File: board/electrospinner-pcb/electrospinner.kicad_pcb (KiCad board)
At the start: 2 copper layers, 28 parts, among them U1 FT230XS, U2 A4988SETTR-T, U3 MSP430G2553IPW20

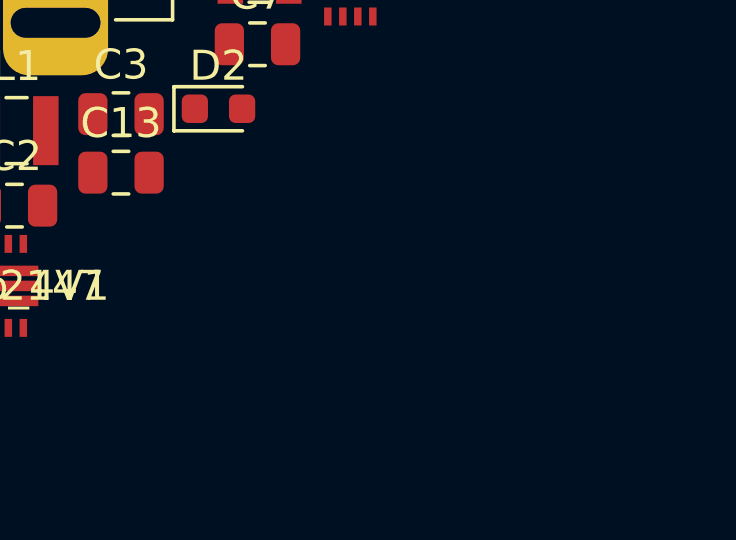
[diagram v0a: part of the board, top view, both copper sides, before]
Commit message: Adds last of the footprints to pcb layout
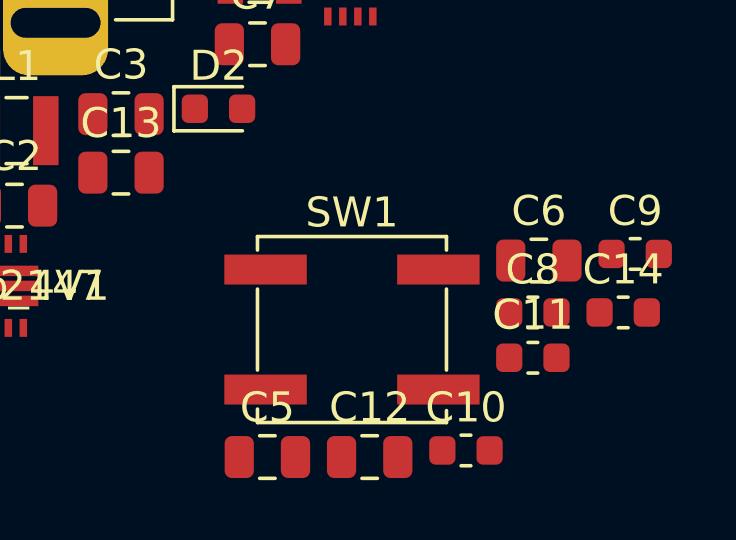
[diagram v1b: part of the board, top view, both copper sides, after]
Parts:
- added C10: 0.1uF, Capacitor_SMD:C_0603_1608Metric, F.Cu at (170.9, 124.1)
- added C11: 0.22uF, Capacitor_SMD:C_0603_1608Metric, F.Cu at (173.1, 121.1)
- added C12: 1uF, Capacitor_SMD:C_0805_2012Metric, F.Cu at (167.7, 124.4)
- added C14: 0.1uF, Capacitor_SMD:C_0603_1608Metric, F.Cu at (176.1, 119.5)
- added C5: 3.3uF, Capacitor_SMD:C_0805_2012Metric, F.Cu at (164.3, 124.4)
- added C6: 3.3uF, Capacitor_SMD:C_0805_2012Metric, F.Cu at (173.3, 117.8)
- added C8: 0.1uF, Capacitor_SMD:C_0603_1608Metric, F.Cu at (173.1, 119.5)
- added C9: 0.1uF, Capacitor_SMD:C_0603_1608Metric, F.Cu at (176.5, 117.6)
- added SW1: ResetBTN, Button_Switch_SMD:SW_SPST_EVPBF, F.Cu at (167.1, 120.1)

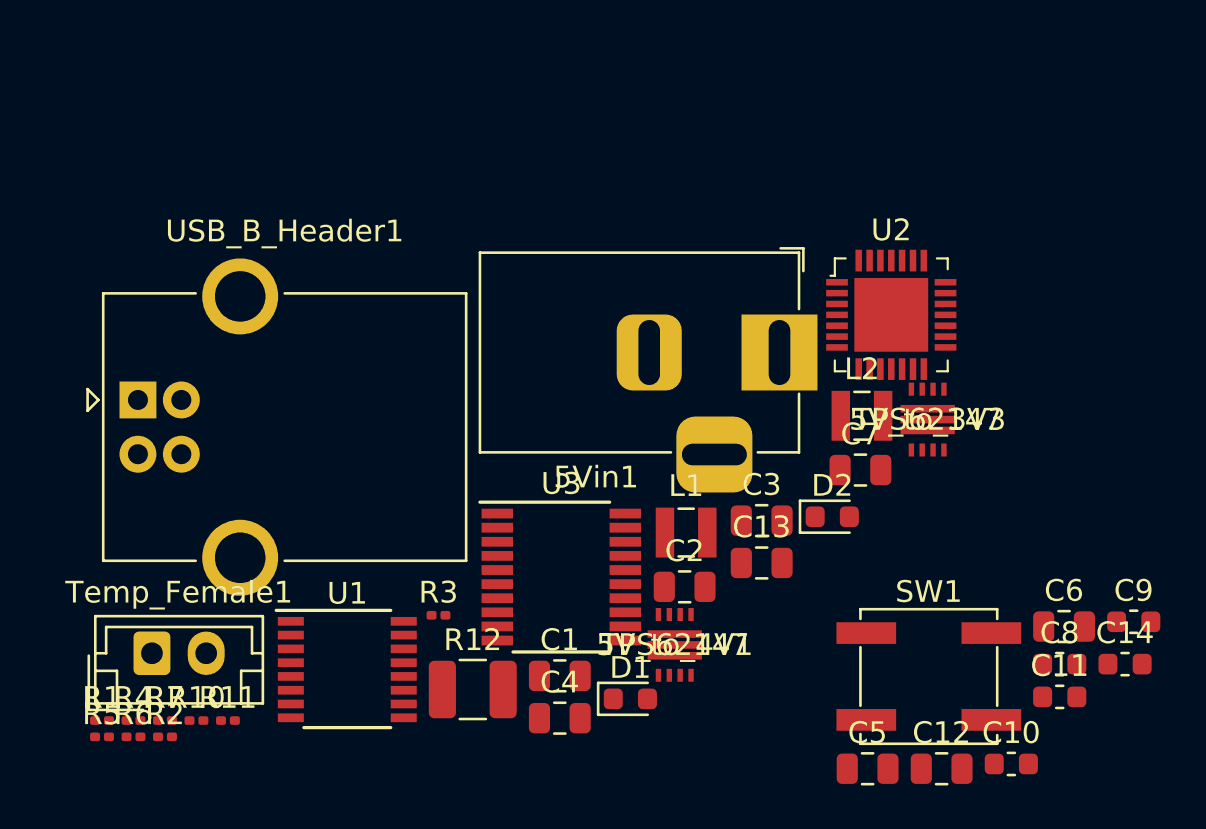
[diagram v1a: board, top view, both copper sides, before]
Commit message: Removes sense resistors from stepper driver
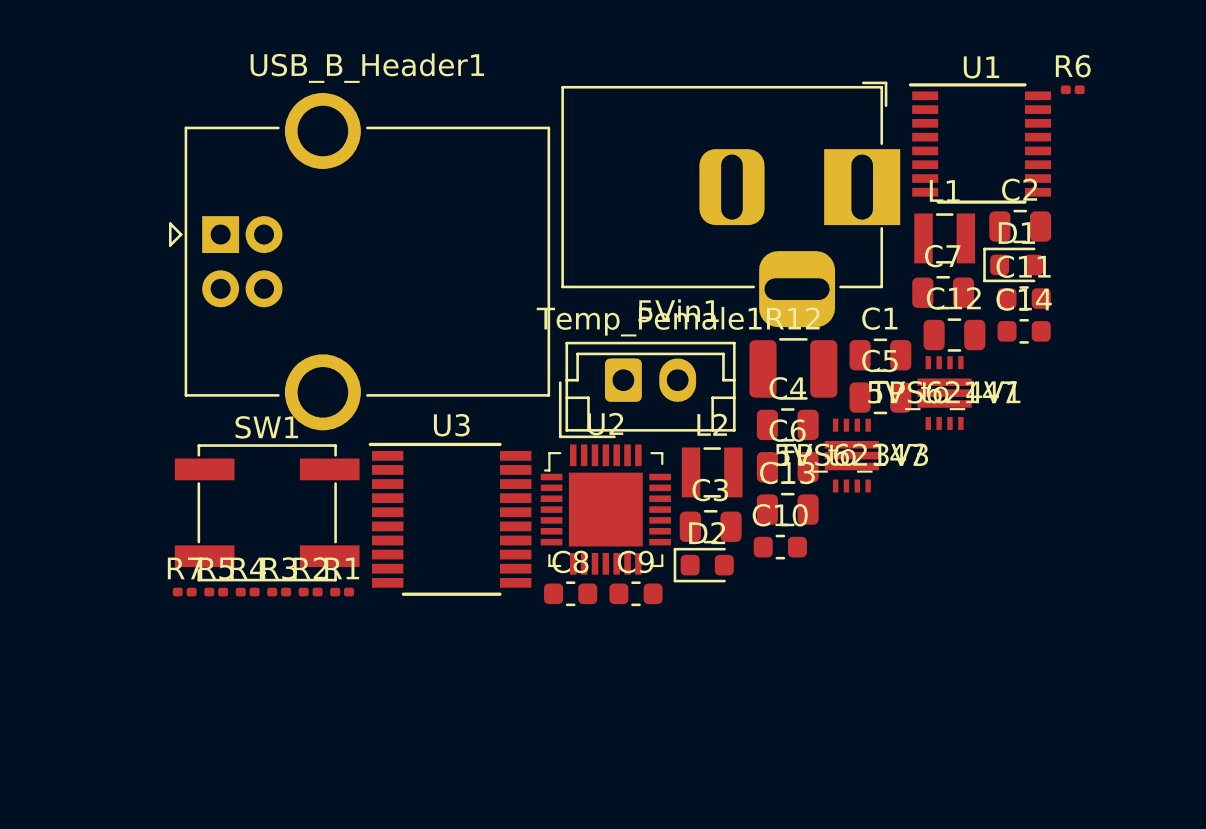
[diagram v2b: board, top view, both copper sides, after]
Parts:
- removed R10, R11: ?k, Resistor_SMD:R_0201_0603Metric
- moved R6 52.5 mm to (173.7, 93.1)
- moved U1 37.9 mm to (169.5, 95.6)
- moved SW1 31.4 mm to (136.6, 112.6)
- moved D1 26.8 mm to (171.1, 101.2)
- moved Temp_Female1 25.1 mm to (153.0, 106.5)
- moved C9 23.0 mm to (153.6, 116.3)
- moved C8 22.8 mm to (150.6, 116.3)
- moved C2 22.7 mm to (171.3, 99.4)
- moved R12 20.9 mm to (160.8, 105.9)
- moved C1 20.9 mm to (164.9, 105.3)
- moved C12 20.0 mm to (168.3, 104.4)
- moved C11 18.4 mm to (171.5, 102.7)
- moved L1 18.0 mm to (167.8, 99.9)
- moved C4 17.1 mm to (160.6, 108.5)
- moved C5 17.1 mm to (164.9, 107.3)
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
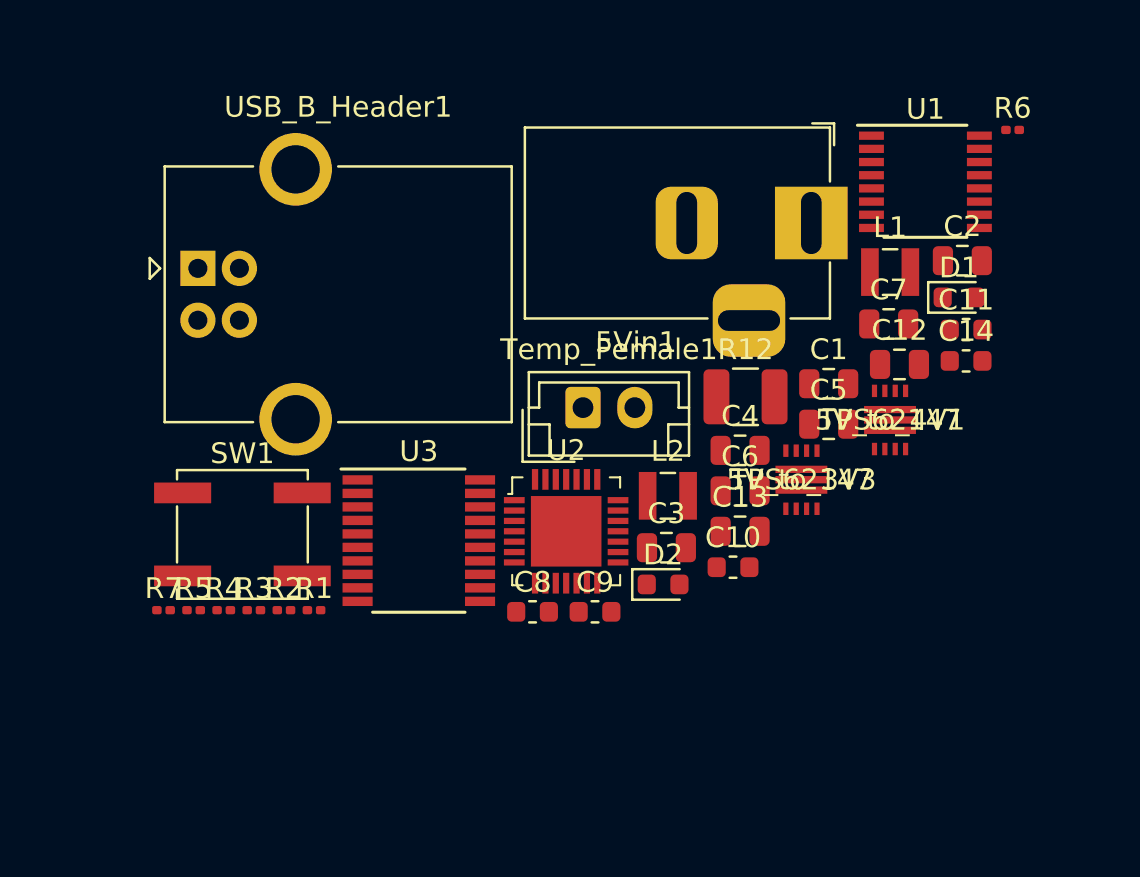
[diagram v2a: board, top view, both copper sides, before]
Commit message: Updates footprints, adds bom
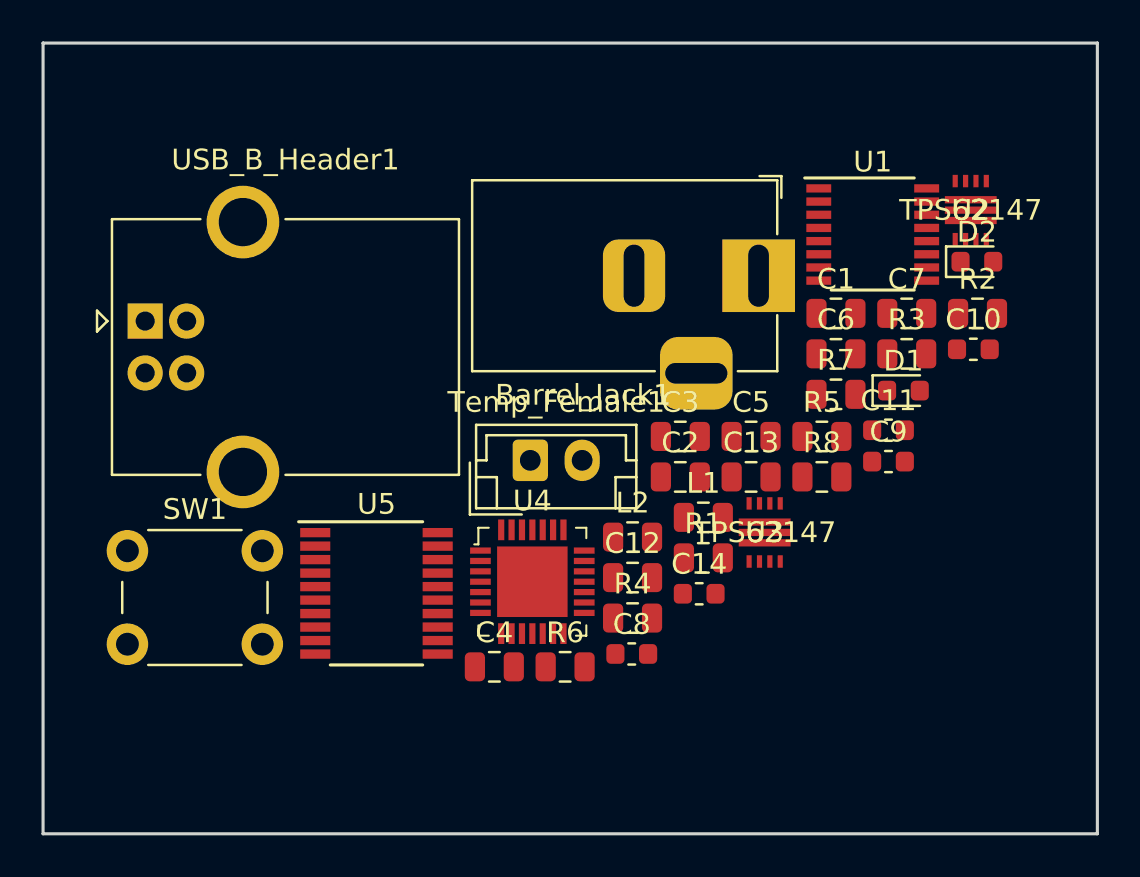
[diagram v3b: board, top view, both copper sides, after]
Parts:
- removed 5V_to_3V3, 5V_to_4V1: TPS62147, footprints:TPS62147RGXR
- removed 5Vin1: BarrelJack, Connector_BarrelJack:BarrelJack_Horizontal
- removed R12: 158, Resistor_SMD:R_1210_3225Metric
- added Barrel_Jack1: BarrelJack, Connector_BarrelJack:BarrelJack_Horizontal, F.Cu at (161.5, 100.1)
- added R8: 158, Resistor_SMD:R_0805_2012Metric, F.Cu at (164.5, 109.8)
- added U4: A4988SETTR-T, digikey-footprints:VFQFN-28-1EP_5x5mm, F.Cu at (150.6, 114.9)
- added U5: MSP430G2553IPW20, Package_SO:TSSOP-20_4.4x6.5mm_P0.65mm, F.Cu at (143.1, 115.4)
- C3, C4: value 2uF -> 3.3uF
- C5, C6: value 3.3uF -> 2uF
- L1, L2: footprint Inductor_SMD:L_Wuerth_MAPI-2510 -> Inductor_SMD:L_0805_2012Metric
- R1: value 560k -> 470k; footprint Resistor_SMD:R_0201_0603Metric -> Resistor_SMD:R_0805_2012Metric
- R2: value 150k -> 100k; footprint Resistor_SMD:R_0201_0603Metric -> Resistor_SMD:R_0805_2012Metric
- R3: value 471k -> 560k; footprint Resistor_SMD:R_0201_0603Metric -> Resistor_SMD:R_0805_2012Metric
- R4: value 100k -> 150k; footprint Resistor_SMD:R_0201_0603Metric -> Resistor_SMD:R_0805_2012Metric
- R5, R6, R7: footprint Resistor_SMD:R_0201_0603Metric -> Resistor_SMD:R_0805_2012Metric
- SW1: footprint Button_Switch_SMD:SW_SPST_EVPBF -> Button_Switch_THT:SW_PUSH_6mm_H5mm
- U2: value A4988SETTR-T -> TPS62147; footprint digikey-footprints:VFQFN-28-1EP_5x5mm -> footprints:TPS62147RGXR
- U3: value MSP430G2553IPW20 -> TPS62147; footprint Package_SO:TSSOP-20_4.4x6.5mm_P0.65mm -> footprints:TPS62147RGXR
- USB_B_Header1: value USB_B -> USB_B_Header?
- moved R2 36.4 mm to (172.0, 101.9)
- moved R7 34.0 mm to (165.2, 105.8)
- moved R3 33.8 mm to (168.6, 103.9)
- moved R6 33.7 mm to (152.2, 119.0)
- moved R5 31.4 mm to (164.5, 107.9)
- moved U2 24.9 mm to (171.7, 96.9)
- moved D2 21.7 mm to (172.0, 99.4)
- moved R4 19.7 mm to (155.4, 116.6)
- moved R1 18.9 mm to (158.8, 113.7)
- moved C2 17.1 mm to (157.7, 109.8)
- moved C14 17.1 mm to (158.6, 115.4)
- moved U3 16.7 mm to (161.8, 112.5)
- moved C12 16.5 mm to (155.4, 114.7)
- moved C9 15.9 mm to (167.7, 109.1)
- moved C4 15.8 mm to (148.7, 119.0)
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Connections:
- C3 pad 1: +3V3 -> Net-(C3-Pad1)
- C4 pad 1: +4V -> Net-(C4-Pad1)
- C5 pad 1: Net-(5V_to_4V1-Pad9) -> +4V
- C6 pad 1: Net-(5V_to_3V3-Pad9) -> +3V3
- L1 pad 1: Net-(5V_to_3V3-Pad2) -> Net-(L1-Pad1)
- L1 pad 2: +3V3 -> +4V
- L2 pad 1: Net-(5V_to_4V1-Pad2) -> Net-(L2-Pad1)
- L2 pad 2: +4V -> +3V3
- R1 pad 1: +3V3 -> +4V
- R1 pad 2: Net-(5V_to_3V3-Pad5) -> Net-(R1-Pad2)
- R2 pad 1: Net-(5V_to_3V3-Pad5) -> Net-(R1-Pad2)
- R3 pad 1: +4V -> +3V3
- R3 pad 2: Net-(5V_to_4V1-Pad5) -> Net-(R3-Pad2)
- R4 pad 1: Net-(5V_to_4V1-Pad5) -> Net-(R3-Pad2)
- U2 pad 1: /2B -> +5V
- U2 pad 10: /MotorMS2 -> GNDD
- U2 pad 11: /MotorMS3 -> +5V
- U2 pad 2: /~MotorENABLE -> Net-(L1-Pad1)
- U2 pad 4: Net-(C9-Pad2) -> GNDD
- U2 pad 5: Net-(C9-Pad1) -> Net-(R1-Pad2)
- U2 pad 6: /VCP -> Net-(L1-Pad1)
- U2 pad 7: Net-(U2-Pad7) -> GNDD
- U2 pad 8: Net-(C11-Pad1) -> +5V
- U2 pad 9: /MotorMS1 -> Net-(C3-Pad1)
- U3 pad 1: +3V3 -> +5V
- U3 pad 10: /MotorMS1 -> GNDD
- U3 pad 11: /MotorMS2 -> +5V
- U3 pad 2: /Vo,temp -> Net-(L2-Pad1)
- U3 pad 3: /PCB_TX -> GNDD
- U3 pad 4: /PCB_RX -> GNDD
- U3 pad 5: Net-(U3-Pad5) -> Net-(R3-Pad2)
- U3 pad 6: Net-(U3-Pad6) -> Net-(L2-Pad1)
- U3 pad 7: Net-(U3-Pad7) -> GNDD
- U3 pad 8: /~MotorSLEEP -> +5V
- U3 pad 9: /MotorSTEP -> Net-(C4-Pad1)
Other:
- board outline added: 50.8 x 38.1 mm

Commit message: Updates BOM and footprints, adds spreadsheet
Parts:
- C10, C11, C14, C8, C9: footprint Capacitor_SMD:C_0603_1608Metric -> Capacitor_SMD:C_0805_2012Metric
- C5, C6: value 2uF -> 2.2uF
- moved C12 24.4 mm to (172.2, 96.9)
- moved C6 21.5 mm to (148.7, 117.7)
- moved C1 20.5 mm to (152.2, 117.7)
- moved C3 19.4 mm to (172.2, 95.0)
- moved C8 18.6 mm to (165.2, 102.6)
- moved D1 17.4 mm to (155.4, 117.1)
- moved D2 16.2 mm to (162.1, 112.3)
- moved L2 15.5 mm to (165.2, 100.7)
- moved C4 13.7 mm to (157.7, 108.5)
- moved C11 13.6 mm to (155.4, 113.4)
- moved U2 11.1 mm to (167.5, 107.2)
- moved R7 9.84 mm to (172.2, 98.9)
- moved C9 9.03 mm to (158.8, 110.5)
- moved C7 8.83 mm to (161.1, 106.6)
- moved R1 7.70 mm to (164.5, 108.5)
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
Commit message: Finishes rev2 of schematic
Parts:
- removed C11: 0.22uF, Capacitor_SMD:C_0805_2012Metric
- removed C12: 1uF, Capacitor_SMD:C_0805_2012Metric
- removed C13: 10uF, Capacitor_SMD:C_0805_2012Metric
- removed C14: 0.1uF, Capacitor_SMD:C_0805_2012Metric
- removed L1: 1uH, Inductor_SMD:L_0805_2012Metric
- removed R1: 470k, Resistor_SMD:R_0805_2012Metric
- removed R8: 158, Resistor_SMD:R_0805_2012Metric
- removed U2, U3: TPS62147, footprints:TPS62147RGXR
- removed U4: A4988SETTR-T, digikey-footprints:VFQFN-28-1EP_5x5mm
- added A1: Pololu_Breakout_A4988-Driver_Motor, Module:Pololu_Breakout-16_15.2x20.3mm, F.Cu at (128.6, 93.0)
- added J1: Header_02x02, Connector_PinHeader_1.00mm:PinHeader_2x02_P1.00mm_Vertical, F.Cu at (168.0, 108.4)
- C1: value 10uF -> 0.1uF
- C10, C8, C9: footprint Capacitor_SMD:C_0805_2012Metric -> Capacitor_SMD:C_0603_1608Metric
- C3: value 3.3uF -> 100uF; footprint Capacitor_SMD:C_0805_2012Metric -> Capacitor_SMD:CP_Elec_6.3x5.8
- C5: value 2.2uF -> 0.1uF; footprint Capacitor_SMD:C_0805_2012Metric -> Capacitor_SMD:C_0603_1608Metric
- C7: value 10uF -> 0.1uF; footprint Capacitor_SMD:C_0805_2012Metric -> Capacitor_SMD:C_0603_1608Metric
- R2: value 100k -> 100
- R7: value 1k -> 10k
- moved D2 24.9 mm to (138.1, 119.0)
- moved C2 22.2 mm to (138.3, 117.2)
- moved C4 20.6 mm to (138.3, 115.2)
- moved U5 19.9 mm to (162.8, 111.6)
- moved C10 19.1 mm to (160.3, 117.9)
- moved C5 18.4 mm to (170.8, 101.3)
- moved R6 17.6 mm to (169.2, 104.4)
- moved C1 16.8 mm to (162.4, 104.4)
- moved Temp_Female1 15.0 mm to (163.7, 100.7)
- moved Barrel_Jack1 14.8 mm to (156.8, 112.9)
- moved D1 14.4 mm to (141.1, 119.0)
- moved C7 13.7 mm to (173.8, 101.3)
- moved USB_B_Header1 13.5 mm to (145.2, 98.5)
- moved C6 11.4 mm to (138.3, 113.3)
- moved C9 11.1 mm to (169.0, 106.1)
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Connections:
- Barrel_Jack1 pad 1: +5V -> +12V
- C1 pad 1: +5V -> +12V
- C10 pad 1: +4V -> +3V3
- C10 pad 2: GNDD -> Net-(C10-Pad2)
- C2 pad 1: +5V -> +12V
- C3 pad 1: Net-(C3-Pad1) -> +12V
- C5 pad 1: +4V -> +3V3
- C8 pad 1: GNDD -> +3V3
- C8 pad 2: +3V3 -> GNDD
- C9 pad 1: Net-(C9-Pad1) -> +3V3
- C9 pad 2: Net-(C9-Pad2) -> GNDD
- R2 pad 1: Net-(R1-Pad2) -> /~RST
- R2 pad 2: GNDD -> Net-(C10-Pad2)
- R7 pad 1: Net-(R7-Pad1) -> /~RST
- SW1 pad 1: Net-(R7-Pad1) -> /~RST
- U5 pad 15: /~MotorLABEL -> /~MotorSLEEP
- U5 pad 16: Net-(R7-Pad1) -> /~RST
- U5 pad 17: Net-(U5-Pad17) -> /TEST

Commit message: Add files via upload
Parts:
- moved A1 62.2 mm to (182.9, 123.2), turned to 270 degrees
- moved SW1 48.2 mm to (176.5, 109.2)
- moved D2 41.7 mm to (176.5, 102.9)
- moved D1 40.0 mm to (176.5, 100.3)
- moved C3 35.6 mm to (149.9, 127.0)
- moved C1 33.9 mm to (149.9, 135.9)
- moved L2 26.8 mm to (156.2, 121.9)
- moved USB_B_Header1 25.0 mm to (170.2, 97.8), turned to 180 degrees
- moved R7 20.2 mm to (171.4, 118.1), turned to 270 degrees
- moved R3 20.2 mm to (144.8, 96.5)
- moved C10 20.2 mm to (180.3, 120.7)
- moved R2 20.0 mm to (180.3, 118.1)
- moved Temp_Female1 17.8 mm to (146.1, 102.9)
- moved R5 15.7 mm to (180.3, 100.3), turned to 180 degrees
- moved C9 15.5 mm to (184.2, 102.9)
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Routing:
- net +3V3: track 0.00 -> 88.7 mm, vias 0 -> 3
- net GNDD: track 0.00 -> 74.9 mm
- net /~RST: track 0.00 -> 33.1 mm
- net /PCB_RX: track 0.00 -> 24.1 mm, vias 0 -> 2
- net /PCB_TX: track 0.00 -> 23.8 mm, vias 0 -> 2
- net /D-: track 0.00 -> 19.7 mm
- net /Vo,temp: track 0.00 -> 17.8 mm
- net +12V: track 0.00 -> 16.6 mm
- net /~RXLED: track 0.00 -> 8.46 mm
- net /D+: track 0.00 -> 7.92 mm
- net /~TXLED: track 0.00 -> 7.74 mm
- net /TEST: track 0.00 -> 4.16 mm
- net Net-(C10-Pad2): track 0.00 -> 2.60 mm
- net Net-(D2-Pad2): track 0.00 -> 2.09 mm
- net Net-(D1-Pad2): track 0.00 -> 2.09 mm
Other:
- board outline removed

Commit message: Updates board to rev 3
Updates thematic
Updates bom
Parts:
- A1: value Pololu_Breakout_A4988-Driver_Motor -> A4988_Breakout
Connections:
- U5 pad 15: /~MotorSLEEP -> /~MotorRESET
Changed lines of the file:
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@@
-(kicad_pcb (version 20171130) (host pcbnew "(5.1.0)-1")
+(kicad_pcb (version 20171130) (host pcbnew 5.1.0)
   (general
     (thickness 1.6)
@@
     (zones 0)
     (modules 27)
-    (nets 51)
+    (nets 52)
   )
   (page A4)
@@
   (net 49 /DVSS)
   (net 50 /TEST)
+  (net 51 /~MotorRESET)
   (net_class Default "This is the default net class."
     (clearance 0.2)
@@
     (add_net /~MOTOR_SLEEP)
     (add_net /~MotorENABLE)
+    (add_net /~MotorRESET)
     (add_net /~MotorSLEEP)
     (add_net /~RST)
@@
       (effects (font (size 1 1) (thickness 0.15)))
     )
-    (fp_text value Pololu_Breakout_A4988-Driver_Motor (at 6.35 20.17 270) (layer F.Fab)
+    (fp_text value A4988_Breakout (at 6.35 20.17 270) (layer F.Fab)
       (effects (font (size 1 1) (thickness 0.15)))
     )
@@
       (net 23 /~MotorENABLE))
     (pad 15 smd rect (at 2.95 0.325) (size 1.45 0.45) (layers F.Cu F.Paste F.Mask)
-      (net 27 /~MotorSLEEP))
+      (net 51 /~MotorRESET))
     (pad 16 smd rect (at 2.95 -0.325) (size 1.45 0.45) (layers F.Cu F.Paste F.Mask)
       (net 5 /~RST))
@@
   (via (at 182.88 95.25) (size 0.8) (drill 0.4) (layers F.Cu B.Cu) (net 1))
   (via (at 162.56 105.41) (size 0.8) (drill 0.4) (layers F.Cu B.Cu) (net 1))
-  (via (at 162.56 107.95) (size 0.8) (drill 0.4) (layers F.Cu B.Cu) (net 8))
-  (via (at 173 93.98) (size 0.8) (drill 0.4) (layers F.Cu B.Cu) (net 8))
-  (via (at 162.56 109.22) (size 0.8) (drill 0.4) (layers F.Cu B.Cu) (net 10))
-  (via (at 173 95) (size 0.8) (drill 0.4) (layers F.Cu B.Cu) (net 10))
   (segment (start 183.3625 99.06) (end 183.3625 100.33) (width 0.25) (layer F.Cu) (net 1))
   (segment (start 183.3625 100.33) (end 183.3625 101.6) (width 0.25) (layer F.Cu) (net 1))
@@
   (segment (start 179.4025 100.33) (end 177.3175 100.33) (width 0.25) (layer F.Cu) (net 6))
   (segment (start 179.4025 102.87) (end 177.3175 102.87) (width 0.25) (layer F.Cu) (net 7))
+  (via (at 162.56 107.95) (size 0.8) (drill 0.4) (layers F.Cu B.Cu) (net 8))
+  (via (at 173 93.98) (size 0.8) (drill 0.4) (layers F.Cu B.Cu) (net 8))
   (segment (start 173.9525 93.0275) (end 175.2 93.0275) (width 0.25) (layer F.Cu) (net 8))
   (segment (start 173 93.98) (end 173.9525 93.0275) (width 0.25) (layer F.Cu) (net 8))
@@
   (segment (start 172.434315 93.98) (end 171.355001 95.059314) (width 0.25) (layer B.Cu) (net 8))
   (segment (start 173 93.98) (end 172.434315 93.98) (width 0.25) (layer B.Cu) (net 8))
+  (via (at 162.56 109.22) (size 0.8) (drill 0.4) (layers F.Cu B.Cu) (net 10))
+  (via (at 173 95) (size 0.8) (drill 0.4) (layers F.Cu B.Cu) (net 10))
   (segment (start 173.0675 94.9325) (end 173 95) (width 0.25) (layer F.Cu) (net 10))
   (segment (start 175.2 94.9325) (end 173.0675 94.9325) (width 0.25) (layer F.Cu) (net 10))
